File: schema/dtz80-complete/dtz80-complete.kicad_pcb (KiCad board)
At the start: 2 copper layers, 104 parts, among them IC1 Z80SIO, IC2 Z80CTC, J1 FT_232 A, J10 JACK_TRS, J11 YM Parallel IO, J12 Micro USB, J13 Conn_01x01, J14 Conn_01x01, J15 Conn_01x01, J16 Conn_01x01, J17 Conn_01x01, J18 Conn_01x01, J19 Conn_01x01, J1_5VtoSerial1 5V Serial, J2 CTC, J20 Conn_01x01, J21 Conn_01x01, J22 Conn_01x01, J3 LCD Display, J4 8 Bit Output, J5 RC2014Bus, J6 FT_232 B, J7 Enable Lines, J8 External Clock, J9 System Bus, SW1 Reset, U1 74LS32, U10 5161AS, U11 HM62256, U12 NE555P, U13 74LS573, U14 YM2149, U15 74HCT138, U16 74HC00, U2 Z80CPU, U3 28C256, U4 74LS393, U5 74LS04, U6 74LS138, U7 74LS573, U8 74HC245, U9 74LS32, X1 CXO_DIP8, Y1 Crystal

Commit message: full schema
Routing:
- net /D7: track 364.3 -> 581.4 mm, vias 14 -> 33
- net /A15: track 77.2 -> 273.4 mm, vias 1 -> 20
- net GND: track 635.2 -> 830.7 mm, vias 13 -> 23
- net /D5: track 267.6 -> 459.7 mm, vias 9 -> 25
- net /IEI: track 175.9 -> 366.4 mm, vias 14 -> 24
- net /D4: track 291.9 -> 477.9 mm, vias 16 -> 37
- net /A8: track 30.7 -> 214.9 mm, vias 0 -> 15
- net /~RESET~: track 285.9 -> 459.3 mm, vias 15 -> 27
- net /A11: track 66.3 -> 230.1 mm, vias 0 -> 21
- net /A3: track 94.2 -> 257.3 mm, vias 7 -> 26
- net /A10: track 85.7 -> 247.7 mm, vias 0 -> 11
- net /A2: track 119.0 -> 279.3 mm, vias 7 -> 30
- net /D6: track 347.0 -> 505.8 mm, vias 16 -> 34
- net /A12: track 103.9 -> 251.0 mm, vias 10 -> 18
- net /DIV4: track 55.6 -> 190.9 mm, vias 4 -> 15
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
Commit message: Schema completet
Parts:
- added JP10: ROM On, Connector_PinHeader_2.54mm:PinHeader_1x02_P2.54mm_Vertical, F.Cu at (109.9, 106.7)
- added JP11: ROM Off, Connector_PinHeader_2.54mm:PinHeader_1x02_P2.54mm_Vertical, F.Cu at (114.9, 106.7)
- added R34: 10k, Resistor_THT:R_Axial_DIN0207_L6.3mm_D2.5mm_P10.16mm_Horizontal, F.Cu at (128.3, 99.1)
- J3: value LCD Display -> LCD
- moved U3 2.54 mm to (101.6, 121.9)
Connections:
- IC1 pad 10: (no net) -> Net-(IC1-Pad10)
- IC1 pad 16: (no net) -> Net-(IC1-Pad16)
- IC1 pad 25: (no net) -> Net-(IC1-Pad25)
- IC1 pad 30: (no net) -> Net-(IC1-Pad30)
- IC1 pad 7: (no net) -> Net-(IC1-Pad7)
- IC2 pad 12: (no net) -> Net-(IC2-Pad12)
- J1 pad 6: (no net) -> Net-(J1-Pad6)
- J12 pad 2: (no net) -> Net-(J12-Pad2)
- J12 pad 3: (no net) -> Net-(J12-Pad3)
- J12 pad 4: (no net) -> Net-(J12-Pad4)
- J13 pad 1: (no net) -> Net-(J13-Pad1)
- J14 pad 1: (no net) -> Net-(J14-Pad1)
- J15 pad 1: (no net) -> Net-(J15-Pad1)
- J16 pad 1: (no net) -> Net-(J16-Pad1)
- J17 pad 1: (no net) -> Net-(J17-Pad1)
- J18 pad 1: (no net) -> Net-(J18-Pad1)
- J19 pad 1: (no net) -> Net-(J19-Pad1)
- J20 pad 1: (no net) -> Net-(J20-Pad1)
- J21 pad 1: (no net) -> Net-(J21-Pad1)
- J22 pad 1: (no net) -> Net-(J22-Pad1)
- J5 pad 40: (no net) -> Net-(J5-Pad40)
- J6 pad 6: (no net) -> Net-(J6-Pad6)
- J9 pad 35: /RXA -> Net-(J9-Pad35)
- J9 pad 36: /TXA -> Net-(J9-Pad36)
- J9 pad 40: (no net) -> Net-(J9-Pad40)
- U10 pad 3: (no net) -> Net-(U10-Pad3)
- U13 pad 12: (no net) -> Net-(U13-Pad12)
- U13 pad 13: (no net) -> Net-(U13-Pad13)
- U13 pad 14: (no net) -> Net-(U13-Pad14)
- U13 pad 15: (no net) -> Net-(U13-Pad15)
- U14 pad 2: (no net) -> Net-(U14-Pad2)
- U14 pad 26: (no net) -> Net-(U14-Pad26)
- U14 pad 39: (no net) -> Net-(U14-Pad39)
- U14 pad 5: (no net) -> Net-(U14-Pad5)
- U15 pad 10: (no net) -> Net-(U15-Pad10)
- U15 pad 11: (no net) -> Net-(U15-Pad11)
- U15 pad 12: (no net) -> Net-(U15-Pad12)
- U15 pad 13: (no net) -> Net-(U15-Pad13)
- U15 pad 7: (no net) -> Net-(U15-Pad7)
- U2 pad 17: (no net) -> Net-(U2-Pad17)
- U2 pad 18: (no net) -> Net-(U2-Pad18)
- U2 pad 23: (no net) -> Net-(U2-Pad23)
- U2 pad 24: (no net) -> Net-(U2-Pad24)
- U2 pad 28: (no net) -> Net-(U2-Pad28)
- U3 pad 20: /A15 -> Net-(JP10-Pad2)
- U4 pad 6: (no net) -> Net-(U4-Pad6)
- X1 pad 1: (no net) -> Net-(X1-Pad1)
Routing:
- net /DIO5: track 139.2 -> 320.5 mm, vias 3 -> 20
- net /DIO4: track 132.3 -> 300.6 mm, vias 5 -> 22
- net /A9: track 85.0 -> 222.5 mm, vias 3 -> 20
- net GND: track 830.7 -> 958.2 mm, vias 23 -> 37
- net /A6: track 209.1 -> 330.8 mm, vias 13 -> 16
- net /DIO6: track 142.5 -> 256.3 mm, vias 3 -> 11
- net Net-(C1-Pad1): track 23.7 -> 129.3 mm, vias 1 -> 15
- net /DIO7: track 164.4 -> 269.7 mm, vias 4 -> 21
- net /~M1~: track 333.7 -> 436.5 mm, vias 18 -> 31
- net /DIO3: track 120.0 -> 222.8 mm, vias 4 -> 16
- net /DIO0: track 101.4 -> 200.6 mm, vias 2 -> 8
- net +5V: track 1142.3 -> 1238.7 mm, vias 21 -> 28
- net /DIO2: track 118.1 -> 214.2 mm, vias 2 -> 13
- net /DIO1: track 103.8 -> 194.9 mm, vias 2 -> 12
- net /D5: track 459.7 -> 546.8 mm, vias 25 -> 37
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- added copper zone on B.Cu, net GND
- added copper zone on F.Cu, net GND
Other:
- board text added: "dtZ80 Rev 1 2020-2021 by Stefan Ostermann thoster.net/dtz80"

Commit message: gerber files
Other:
- board text added: "+5V"
- board text added: "/Y0 /Y1 /Y2 /Y3 /Y4 /Y5 /Y6 /Y7"
- board text added: "A14 A12 A10 A8 A6 A4 A2 A0 +5v RES IEI WR IOR D1 D3 D5 D7 X /Y6 X A15 A13 A11 A9 A7 A5 A3 A1 GND M1 CLK MRQ RD D0 D2 D4 D6 X /Y5 /Y7"
- board text added: "GND"
- board text added: "GND CTS +5V TX RX DTR"
- board text added: "GND DIO6 DIO0 DIO7 DIO1 AO0 DIO3 AO2 DIO4 AO3 DIO5 +5V"

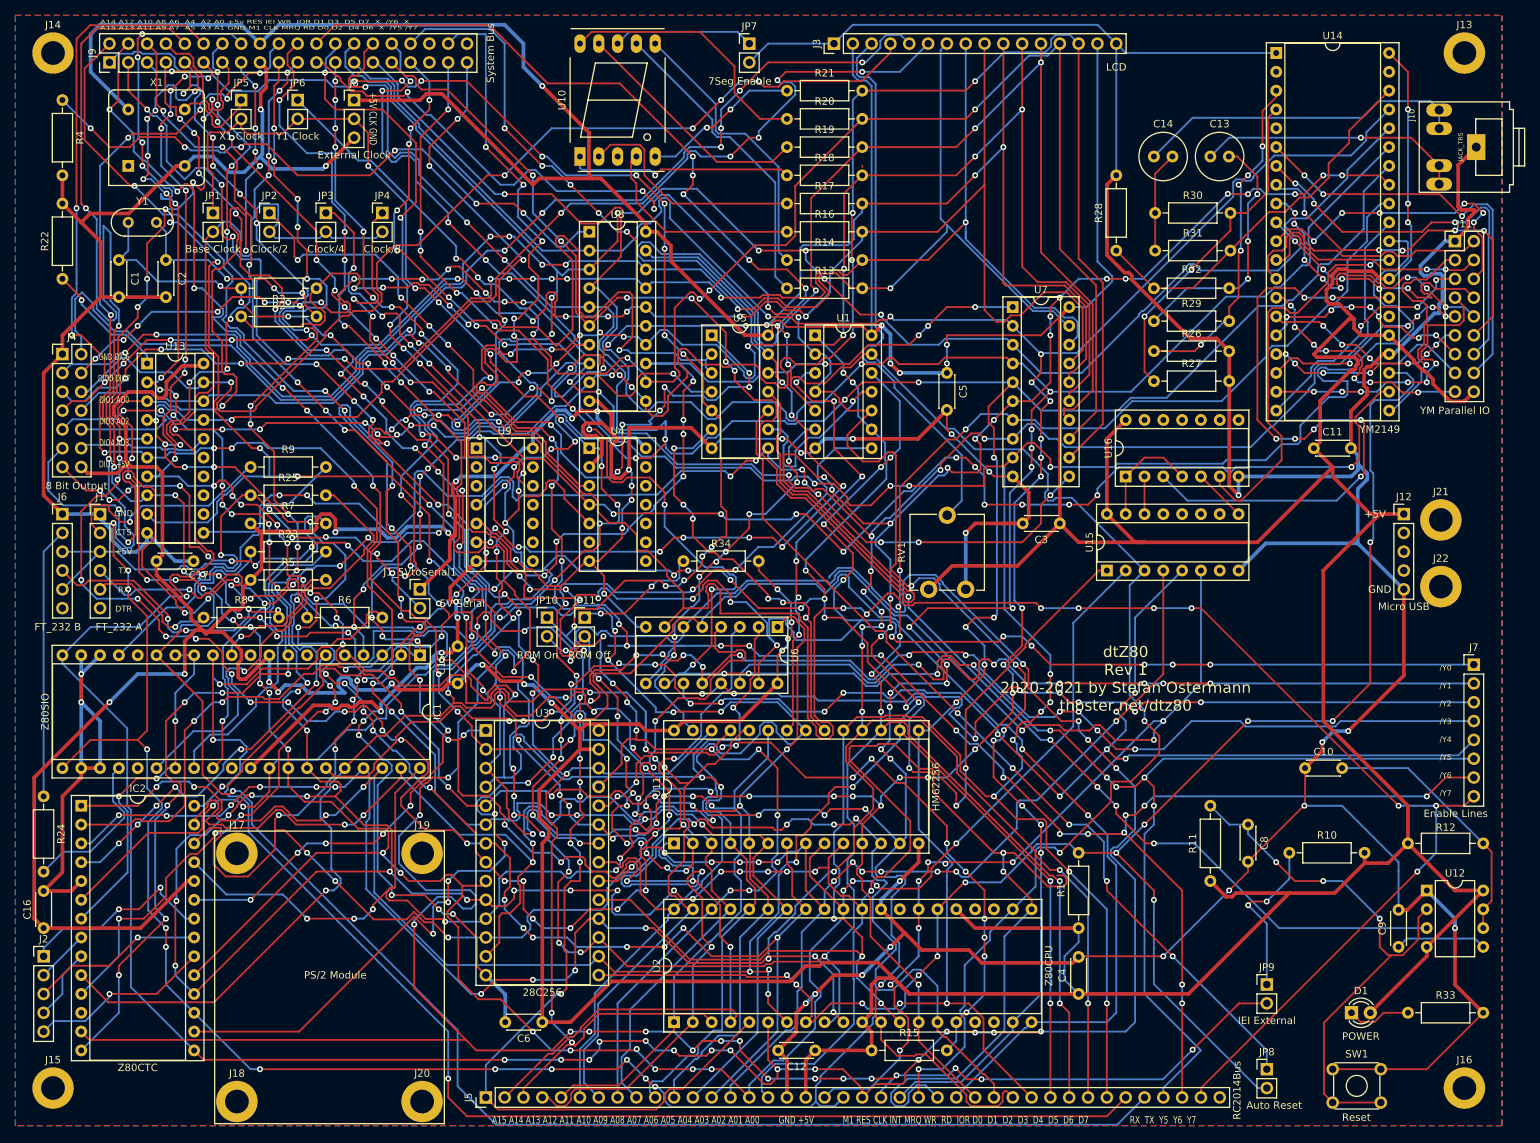
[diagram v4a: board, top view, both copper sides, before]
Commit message: complete schema, first assembler tests
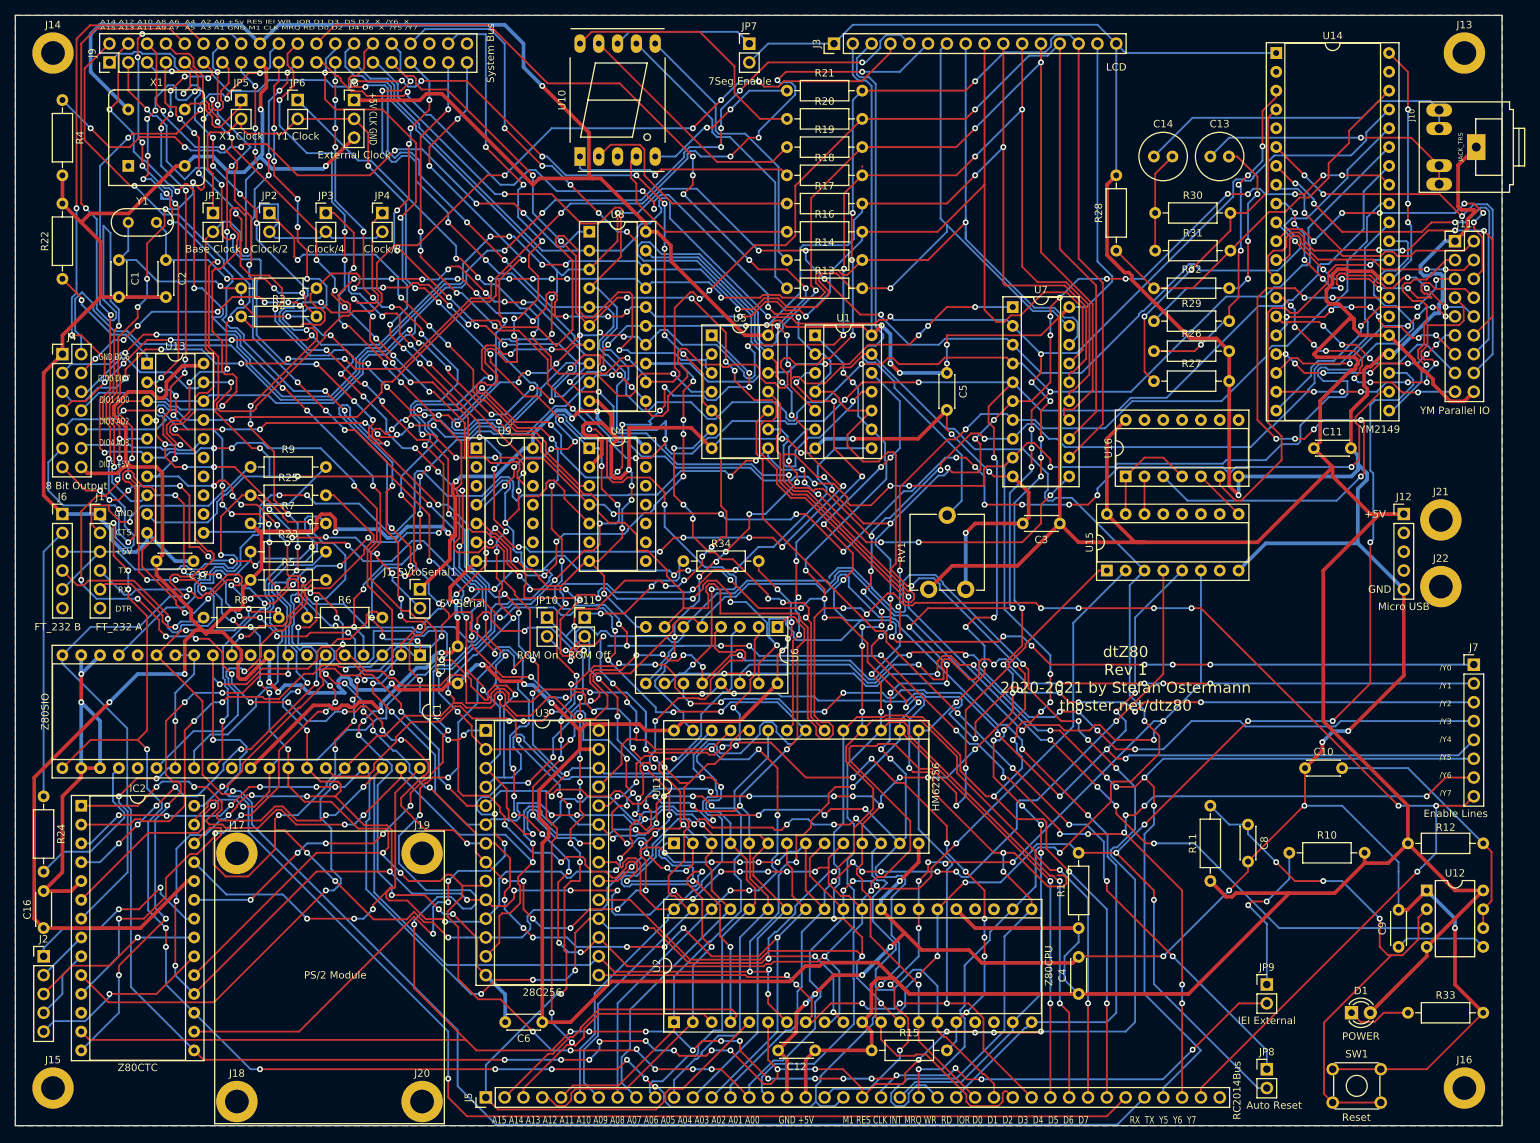
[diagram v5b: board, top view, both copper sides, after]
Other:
- board outline added: 200.7 x 149.9 mm

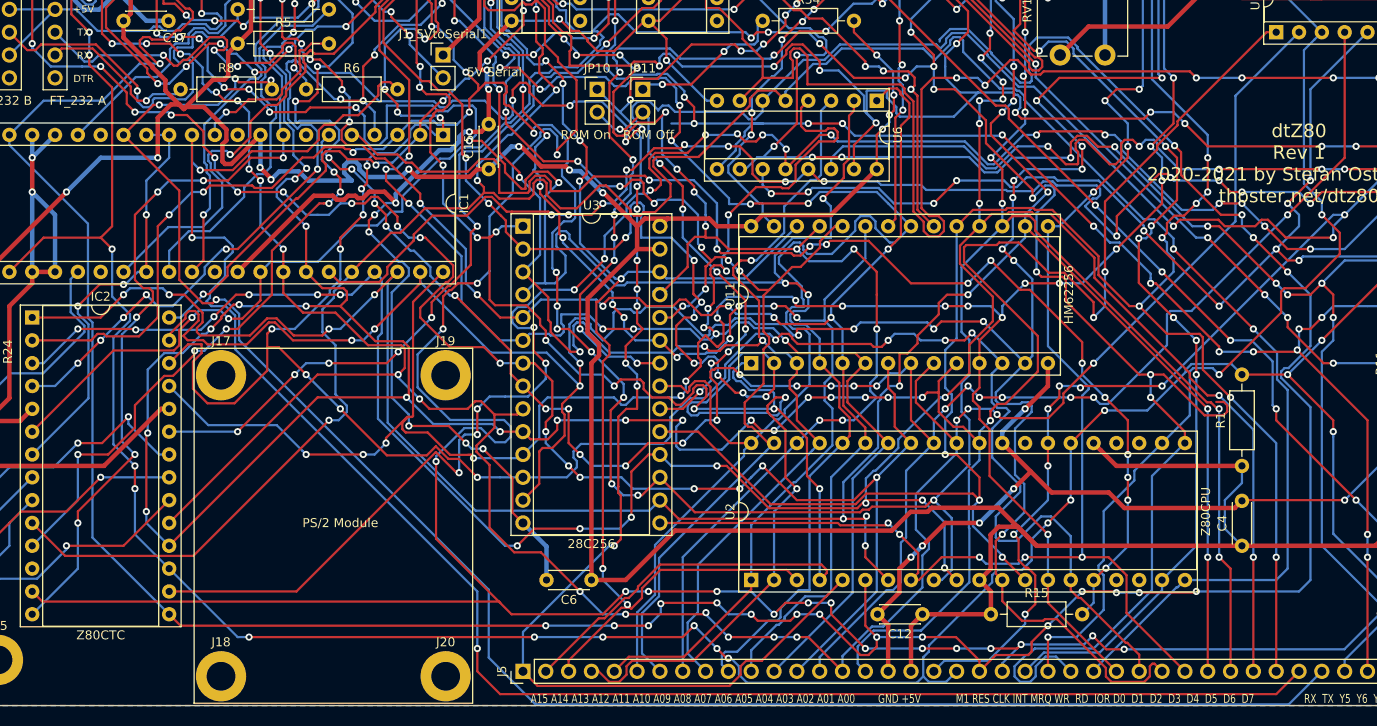
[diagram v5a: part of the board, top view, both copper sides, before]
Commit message: Black dtZ80 complete board and ASM code
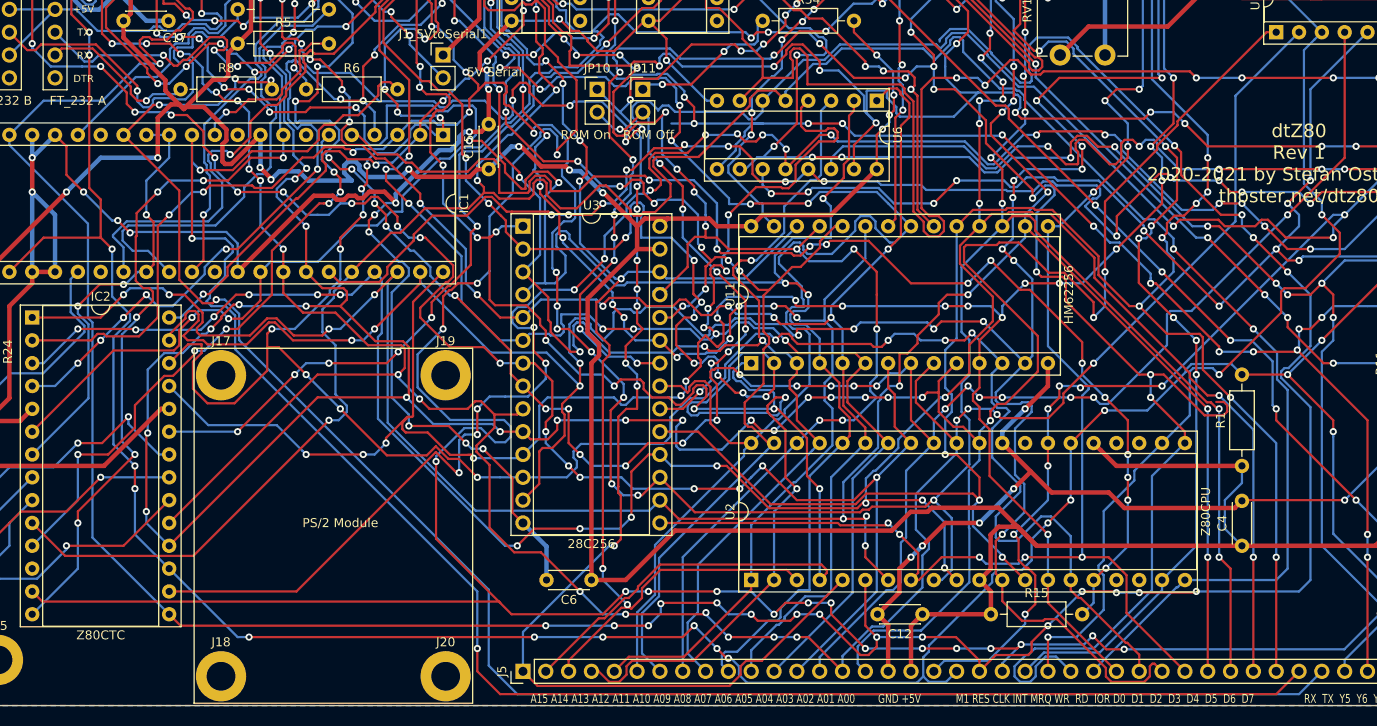
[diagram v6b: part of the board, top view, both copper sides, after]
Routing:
- net GND: track 958.2 -> 988.7 mm, vias 37 -> 40
- net Net-(IC1-Pad28): track 42.5 -> 52.1 mm
- net Net-(IC1-Pad26): track 60.8 -> 64.9 mm
- net /~RESET~: track 470.2 -> 469.2 mm
- net /UART_CLK: track 47.6 -> 48.3 mm
